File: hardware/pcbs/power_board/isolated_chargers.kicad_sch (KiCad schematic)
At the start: 9 parts, among them Q1 BSS138

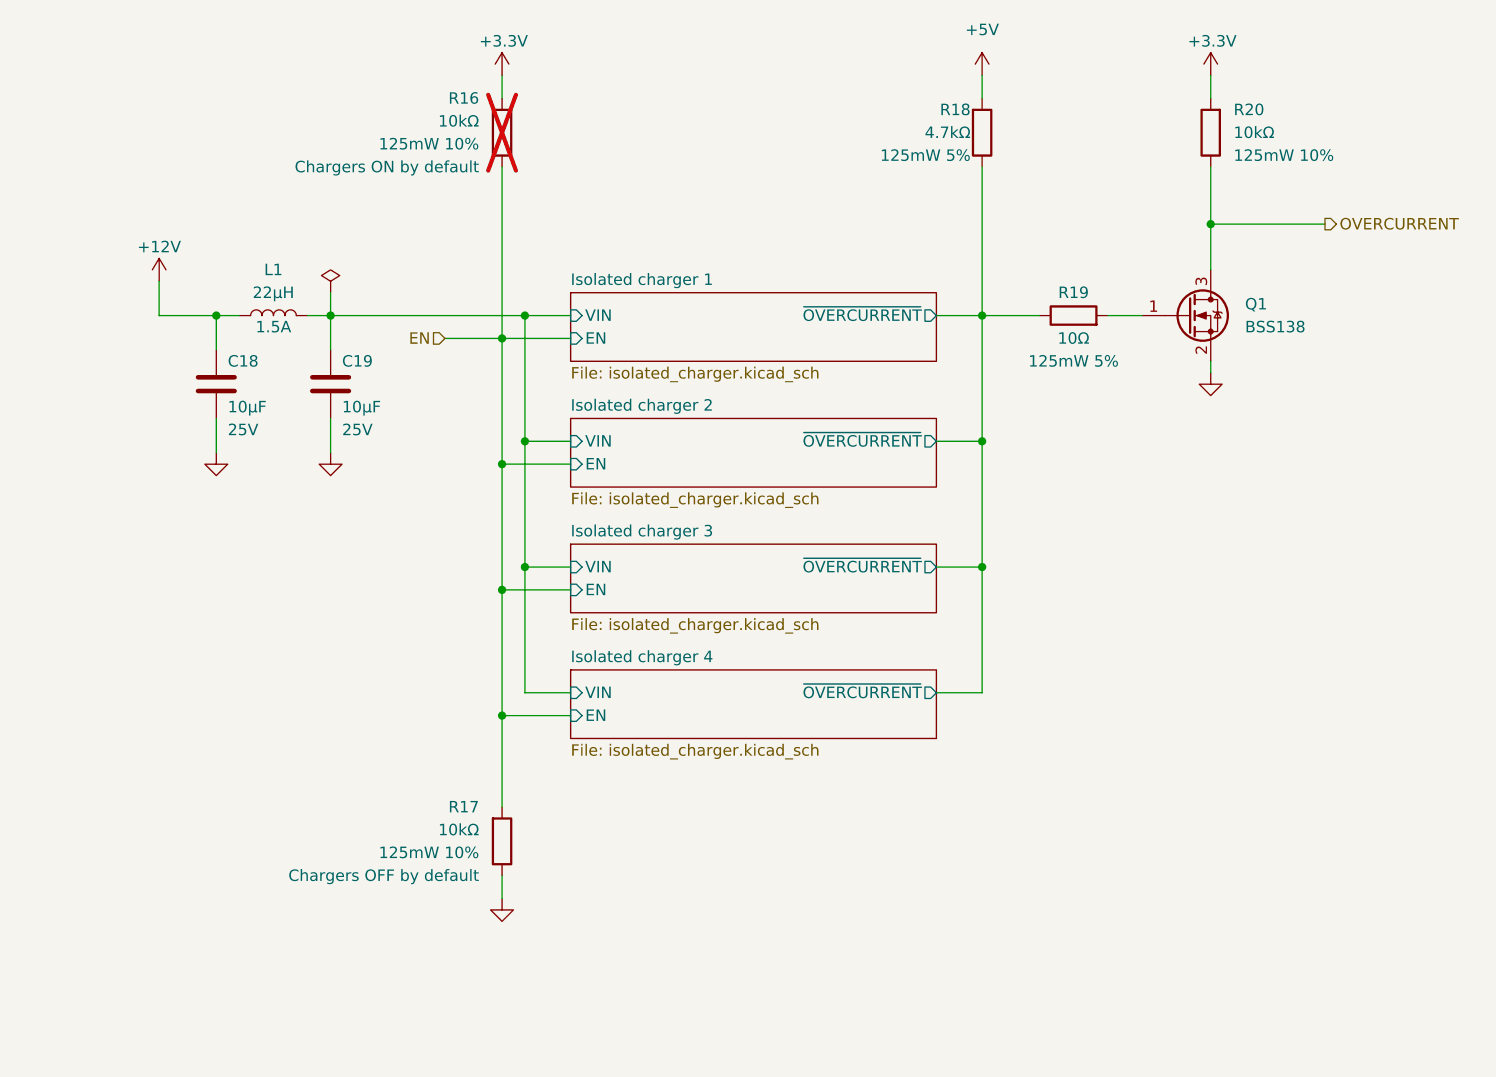
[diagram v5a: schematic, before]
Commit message: audio_board, power_board: update shop and part links
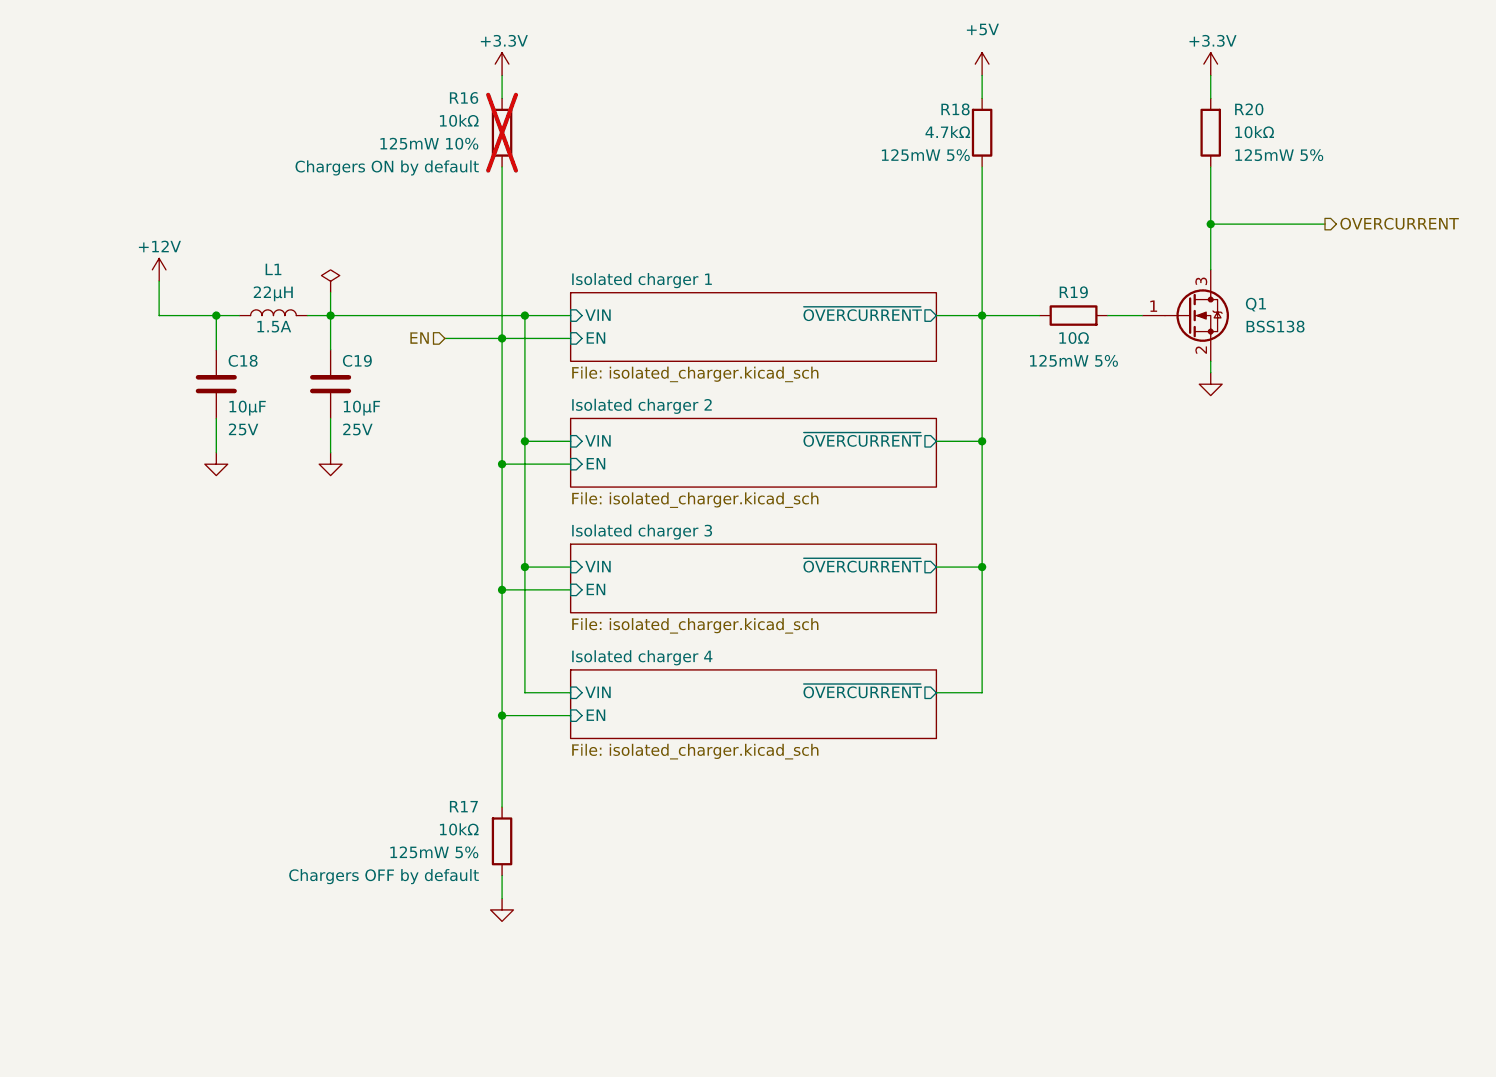
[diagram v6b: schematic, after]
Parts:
- C18, C19: Part (none) -> C 10μF 25V 0805
- R17, R20: Info 125mW 10% -> 125mW 5%; Part (none) -> R 10kΩ 125mW 5% 0805
- R18: Part (none) -> R 4.7kΩ 125mW 5% 0805
- R19: Part (none) -> R 10Ω 125mW 5% 0805
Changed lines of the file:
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@@
+			)
+		)
+		(property "Part" "R 10Ω 125mW 5% 0805"
+			(at 182.88 86.36 0)
+			(effects
+				(font
+					(size 1.27 1.27)
+				)
+				(hide yes)
 			)
 		)
@@
 			)
 		)
-		(property "Info" "125mW 10%"
+		(property "Info" "125mW 5%"
 			(at 116.84 146.05 0)
 			(effects
@@
 			)
 		)
+		(property "Part" "R 10kΩ 125mW 5% 0805"
+			(at 119.38 144.78 0)
+			(effects
+				(font
+					(size 1.27 1.27)
+				)
+				(hide yes)
+			)
+		)
 		(pin "1"
 		)
@@
 		)
 		(property "LCSC" "C15850"
+			(at 100.33 93.98 0)
+			(effects
+				(font
+					(size 1.27 1.27)
+				)
+				(hide yes)
+			)
+		)
+		(property "Part" "C 10μF 25V 0805"
 			(at 100.33 93.98 0)
 			(effects
@@
 			)
 		)
-		(property "Info" "125mW 10%"
+		(property "Info" "125mW 5%"
 			(at 200.66 68.58 0)
 			(effects
@@
 		)
 		(property "LCSC" "C17414"
+			(at 198.12 66.04 0)
+			(effects
+				(font
+					(size 1.27 1.27)
+				)
+				(hide yes)
+			)
+		)
+		(property "Part" "R 10kΩ 125mW 5% 0805"
 			(at 198.12 66.04 0)
 			(effects
@@
 			)
 		)
+		(property "Part" "C 10μF 25V 0805"
+			(at 87.63 93.98 0)
+			(effects
+				(font
+					(size 1.27 1.27)
+				)
+				(hide yes)
+			)
+		)
 		(pin "1"
 		)
@@
 			(at 172.72 66.04 0)
 			(effects
+				(font
+					(size 1.27 1.27)
+				)
+				(hide yes)
+			)
+		)
+		(property "Part" "R 4.7kΩ 125mW 5% 0805"
+			(at 172.72 66.04 0)
+			(effects

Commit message: power_board: BIGGER inductors
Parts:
- R19: value 10Ω -> 10Ω
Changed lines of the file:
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@@
 			)
 		)
-		(property "Value" "10Ω "
+		(property "Value" "10Ω"
 			(at 182.88 88.9 90)
 			(effects
